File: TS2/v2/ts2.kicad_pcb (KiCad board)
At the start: 2 copper layers, 127 x 221 mm, 104 parts, among them P1 FTDI (TERMINAL), P2 FTDI (HOST), P3 +5V POWER, SW1 RESET, SW2 SINGLE STEP/RUN, SW3 STEP, SW4 ABORT, SW5 POWER, U1 555, U10 74LS32, U11 HM6264, U12 28C64, U13 HM6264, U14 28C64, U15 HM6264, U16 28C64, U17 HM6264, U18 28C64, U19 74LS20, U2 8 MHz, U20 74LS74, U21 74LS161, U22 74LS161, U23 74LS74, U24 74LS260, U25 74LS260, U26 74LS138, U27 25LS2548, U28 74LS148, U29 6850, U3 74LS00, U30 6850, U31 MC14411, U32 74LS138, U33 74LS138, U34 74LS00, U35 74LS74, U4 74LS06, U5 74LS04, U6 68000, U7 74LS08, U8 74LS32, U9 74LS32, Y1 1.842MHz

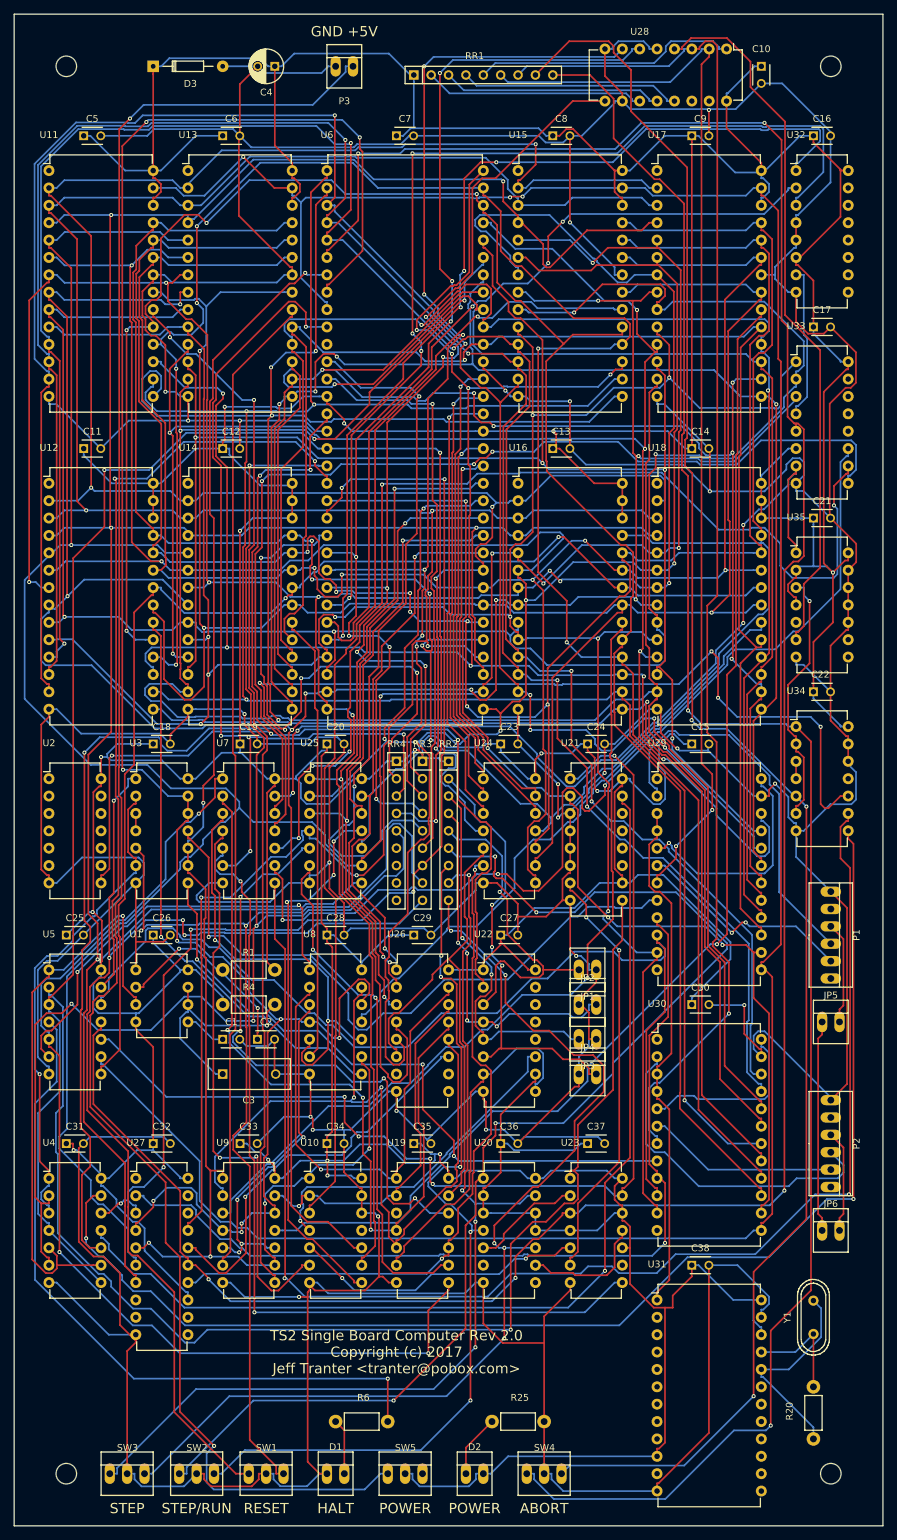
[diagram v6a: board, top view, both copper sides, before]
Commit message: Updated PCB routing.
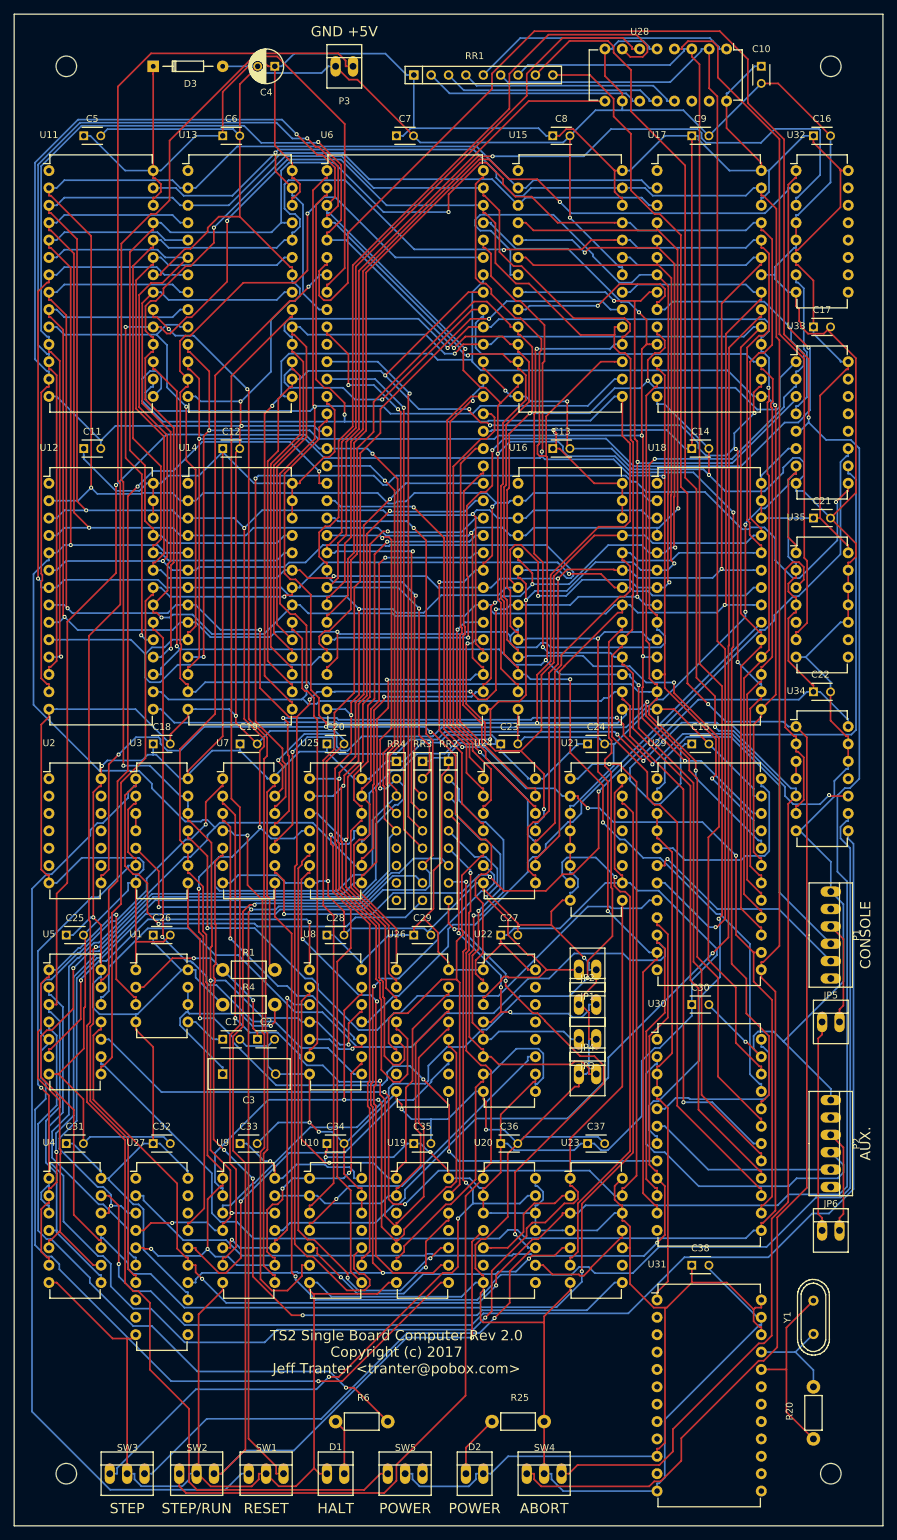
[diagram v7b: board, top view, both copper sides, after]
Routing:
- net Net-(RR2-Pad7): track 130.8 -> 182.1 mm, vias 5 -> 2
- net VCC: track 1344.8 -> 1296.0 mm, vias 15 -> 6
- net Net-(RR2-Pad6): track 180.6 -> 136.4 mm, vias 4 -> 1
- net AS*: track 380.3 -> 420.5 mm, vias 5 -> 3
- net A10: track 299.3 -> 339.3 mm, vias 7 -> 3
- net RESET*: track 202.0 -> 166.6 mm, vias 4 -> 2
- net A07: track 427.9 -> 392.7 mm
- net Net-(RR3-Pad9): track 169.5 -> 202.1 mm, vias 4 -> 1
- net D02: track 322.1 -> 353.8 mm, vias 5 -> 4
- net BERR*: track 191.7 -> 163.6 mm, vias 5 -> 3
- net A01: track 384.7 -> 412.0 mm, vias 9 -> 5
- net BGACK*: track 104.8 -> 78.9 mm, vias 2 -> 1
- net GND: track 1448.8 -> 1424.7 mm, vias 23 -> 14
- net D08: track 250.3 -> 229.0 mm
- net Net-(U34-Pad10): track 132.4 -> 112.0 mm
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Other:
- board text added: "AUX."
- board text added: "CONSOLE"
